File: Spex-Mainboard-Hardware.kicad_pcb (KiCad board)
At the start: 4 copper layers, 94 parts, among them K1 G5LE_1A4_DC3, K2 G5LE_1A4_DC3, P11 SWD Header, P11 USB_OTG, Q11 2N7002K, Q11 BSS215PH6327, Q11 Si5468DC, SW1 SW_PUSH, U1 MKL04Z32VLC4, U11 BME280, U11 LSM9DS1, U11 MCP9808T, U11 MMQA6V2T1G, U11 NUP2201MR6, U111 AT45DB641E, U111 LM4030, U111 MCP2551-I/SN, U111 ST1480ABDR, U13 SCHA4B0419, U3 MK20DX256VLH7, Y11 Crystal

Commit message: Added power board to both sch and pcb. Will route when ready for it
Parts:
- removed C111 (x3), C211: C, Capacitors_SMD:C_0603
- removed C111: .1uF, Capacitors_SMD:C_0603
- removed C111 (x3): 100nF, Capacitors_SMD:C_0603
- removed C111: 10nF, Capacitors_SMD:C_0603
- removed C111: 4.7uF, Capacitors_SMD:C_0603
- removed C111, C211: 10uF, Capacitors_SMD:C_0603
- removed D11 (x4): LED, LEDs:LED_0603
- removed D11 (x2): FM5819-W, Diodes_SMD:SMA_Standard
- removed P11: USB_OTG, Connect:USB_Micro-B
- removed P11: SWD Header, SPEX_Parts:SWD-10
- removed Q11 (x2): 2N7002K, TO_SOT_Packages_SMD:SOT-23
- removed Q11: BSS215PH6327, TO_SOT_Packages_SMD:SOT-23
- removed Q11 (x3): Si5468DC, SPEX_Parts:ChipFet-8
- removed R111 (x2): 1K, Resistors_SMD:R_0603
- removed R111 (x3), R211 (x9): R, Resistors_SMD:R_0603
- removed R111, R211, R311 (x2): 10K, Resistors_SMD:R_0603
- removed R111, R311 (x5): 10k, Resistors_SMD:R_0603
- removed R111 (x3): 12k, Resistors_SMD:R_0603
- removed R311 (x2): 120, Resistors_SMD:R_0603
- removed TH11 (x3): THERMISTOR, Connect:PINHEAD1-2
- removed U111: LM4030, TO_SOT_Packages_SMD:SOT-23-5
- removed U111: MCP2551-I/SN, Power_Integrations:SO-8
- removed U111: ST1480ABDR, Power_Integrations:SO-8
- removed U111: AT45DB641E, SMD_Packages:SOIC-8-N
- removed Y11: Crystal, SPEX_Parts:CX3225GB16000D0HPQCC
- added C1: 1uF, Capacitors_SMD:C_0603, F.Cu at (98.0, -35.6)
- added C10: C, Capacitors_SMD:C_0603, F.Cu at (159.8, -25.8)
- added C105: 47uf, Capacitors_SMD:C_1206, F.Cu at (270.7, -7.50)
- added C109: 100nf, Capacitors_SMD:C_0402, F.Cu at (268.0, 4.40)
- added C114: 22uf, Capacitors_SMD:C_1206, F.Cu at (258.6, -0.90)
- added C118: 22uf, Capacitors_SMD:C_1206, F.Cu at (306.4, -35.0)
- added C119: 1uf 100v, Capacitors_SMD:C_1206, F.Cu at (263.9, -35.0)
- added C12: 10nF, Capacitors_SMD:C_0603, F.Cu at (147.8, -14.1)
- added C120: .1uf 100v, Capacitors_SMD:C_1206, F.Cu at (236.8, -20.9)
- added C121: 100nf, Capacitors_SMD:C_0603, F.Cu at (306.3, -28.7)
- added C122: 47uf, Capacitors_SMD:C_1206, F.Cu at (293.4, -27.1)
- added C123: 1uf 100v, Capacitors_SMD:C_1206, F.Cu at (244.4, -17.4)
- added C13: 100nF, Capacitors_SMD:C_0603, F.Cu at (152.5, -14.1)
- added C14: 4.7uF, Capacitors_SMD:C_0603, F.Cu at (140.4, -10.2)
- added C15: 100nF, Capacitors_SMD:C_0603, F.Cu at (153.1, -20.0)
- added C16: 10uF, Capacitors_SMD:C_0603, F.Cu at (155.9, -25.8)
- added C17: C, Capacitors_SMD:C_0603, F.Cu at (92.4, -13.4)
- added C18: C, Capacitors_SMD:C_0603, F.Cu at (85.9, -6.64)
- added C19: .1uF, Capacitors_SMD:C_0603, F.Cu at (94.8, -19.2)
- added C2: 1uF, Capacitors_SMD:C_0603, F.Cu at (115.0, -56.9)
- added C20: 10uF, Capacitors_SMD:C_0603, F.Cu at (98.7, -19.2)
- added C21: C, Capacitors_SMD:C_0603, F.Cu at (105.9, -46.6)
- added C3: 1uF, Capacitors_SMD:C_0603, F.Cu at (98.0, -41.5)
- added C4: 1uF, Capacitors_SMD:C_0603, F.Cu at (109.3, -51.0)
- added C5: 2.2uF, Capacitors_SMD:C_0603, F.Cu at (119.0, -56.9)
- added C6: .1uF, Capacitors_SMD:C_0603, F.Cu at (108.1, -56.9)
- added C7: C, Capacitors_SMD:C_0603, F.Cu at (94.7, -38.0)
- added C8: C, Capacitors_SMD:C_0603, F.Cu at (111.7, -56.9)
- added C9: C, Capacitors_SMD:C_0603, F.Cu at (152.1, -25.8)
- added D106: ZENER, Diodes_SMD:SOD-123, F.Cu at (253.9, -25.1)
- added D108: ZENER, Diodes_SMD:SOD-123, F.Cu at (262.9, -28.6)
- added D109: D_Schottky_x2_Serial_AKC, Transistors_SMD:sc70, F.Cu at (241.0, -36.3)
- added D110: DIODE, Diodes_SMD:Diode-SMA_Standard, F.Cu at (256.5, -33.5)
- added F101: FUSE, Fuse_Holders_and_Fuses:Fuse_SMD2920, F.Cu at (238.2, -29.6)
- added L102: 2.2uh, SMD_Packages:SMD-2010_Pol, F.Cu at (264.4, -8.88)
- added L103: 3.3uh, NRS8030:NRS8030T3R3MJGJ, F.Cu at (286.1, -25.7)
- added P1: USB_OTG, Connect:USB_Micro-B, F.Cu at (101.4, -55.3)
- added P2: SWD Header, SPEX_Parts:SWD-10, F.Cu at (77.3, -36.9)
- added Q1: 2N7002K, TO_SOT_Packages_SMD:SOT-23, F.Cu at (103.9, -25.5)
- added Q101: MOS_N_numbered, Housings_SOT-23_SOT-143_TSOT-6:SOT-23, F.Cu at (253.9, -7.55)
- added Q104: MOS_N_numbered, Housings_SOT-23_SOT-143_TSOT-6:SOT-23, F.Cu at (288.1, -35.0)
- added Q105: Si3407DV, Power:Si3407DV, F.Cu at (246.3, -23.3)
- added Q106: Q_PNP_BEC, Housings_SOT-23_SOT-143_TSOT-6:SOT-23, F.Cu at (248.1, -31.5)
- added Q2: 2N7002K, TO_SOT_Packages_SMD:SOT-23, F.Cu at (96.6, -25.5)
- added Q3: BSS215PH6327, TO_SOT_Packages_SMD:SOT-23, F.Cu at (77.6, -25.5)
- added Q4: Si5468DC, SPEX_Parts:ChipFet-8, F.Cu at (84.8, -13.5)
- added Q5: Si5468DC, SPEX_Parts:ChipFet-8, F.Cu at (74.9, -9.06)
- added Q6: Si5468DC, SPEX_Parts:ChipFet-8, F.Cu at (87.0, -23.1)
- added R1: R, Resistors_SMD:R_0603, F.Cu at (117.0, -45.2)
- added R10: 1K, Resistors_SMD:R_0603, F.Cu at (104.9, -40.7)
- added R108: 33.2k, Resistors_SMD:R_0603, F.Cu at (275.6, -7.90)
- added R109: 10k, Resistors_SMD:R_0603, F.Cu at (263.3, 1.72)
- added R12: 10K, Resistors_SMD:R_0603, F.Cu at (115.8, -51.0)
- added R126: 10K, Resistors_SMD:R_0603, F.Cu at (267.7, -1.25)
- added R13: 10k, Resistors_SMD:R_0603, F.Cu at (101.4, -41.5)
- added R130: 10K, Resistors_SMD:R_0603, F.Cu at (263.3, -4.13)
- added R14: 12k, Resistors_SMD:R_0603, F.Cu at (134.9, -8.79)
- added R140: 10K, Resistors_SMD:R_0603, F.Cu at (302.8, -22.9)
- added R141: 10K, Resistors_SMD:R_0603, F.Cu at (311.1, -35.4)
- added R145: 10k, Resistors_SMD:R_0603, F.Cu at (298.1, -21.7)
- added R146: 33.2k, Resistors_SMD:R_0603, F.Cu at (254.8, -16.7)
- added R147: 56.2k, Resistors_SMD:R_0603, F.Cu at (298.3, -27.5)
- added R148: 10, Resistors_SMD:R_0603, F.Cu at (267.8, -28.7)
- added R149: 27.4k, Resistors_SMD:R_0603, F.Cu at (274.6, -35.4)
- added R15: 12k, Resistors_SMD:R_0603, F.Cu at (148.8, -20.0)
- added R150: 10, Resistors_SMD:R_0603, F.Cu at (258.7, -22.6)
- added R151: 10.2k, Resistors_SMD:R_0603, F.Cu at (269.9, -35.4)
- added R152: 100k, Resistors_SMD:R_0603, F.Cu at (250.3, -17.8)
- added R16: 12k, Resistors_SMD:R_0603, F.Cu at (131.5, -8.79)
- added R17: R, Resistors_SMD:R_0603, F.Cu at (148.8, -25.8)
- added R18: R, Resistors_SMD:R_0603, F.Cu at (80.1, 8.73)
- added R19: R, Resistors_SMD:R_0603, F.Cu at (83.6, 8.73)
- added R2: 10K, Resistors_SMD:R_0603, F.Cu at (112.3, -39.3)
- added R20: R, Resistors_SMD:R_0603, F.Cu at (87.0, 2.88)
- added R21: R, Resistors_SMD:R_0603, F.Cu at (90.5, 2.88)
- added R22: R, Resistors_SMD:R_0603, F.Cu at (87.0, 8.73)
- added R23: R, Resistors_SMD:R_0603, F.Cu at (73.2, 8.73)
- added R24: R, Resistors_SMD:R_0603, F.Cu at (90.5, 8.73)
- added R25: R, Resistors_SMD:R_0603, F.Cu at (80.1, 2.88)
- added R26: R, Resistors_SMD:R_0603, F.Cu at (76.7, 8.73)
- added R27: R, Resistors_SMD:R_0603, F.Cu at (83.6, 2.88)
- added R28: R, Resistors_SMD:R_0603, F.Cu at (82.5, -6.64)
- added R29: 10K, Resistors_SMD:R_0603, F.Cu at (109.3, -25.8)
- added R3: 33, Resistors_SMD:R_0603, F.Cu at (109.1, -39.3)
- added R30: 10k, Resistors_SMD:R_0603, F.Cu at (89.4, -6.64)
- added R31: 10k, Resistors_SMD:R_0603, F.Cu at (95.8, -13.4)
- added R32: 120, Resistors_SMD:R_0603, F.Cu at (102.6, -19.2)
- added R33: 120, Resistors_SMD:R_0603, F.Cu at (109.3, -20.0)
- added R34: 10K, Resistors_SMD:R_0603, F.Cu at (99.3, -13.4)
- added R35: 10k, Resistors_SMD:R_0603, F.Cu at (92.8, -7.50)
- added R36: 10k, Resistors_SMD:R_0603, F.Cu at (112.8, -25.8)
- added R37: 10k, Resistors_SMD:R_0603, F.Cu at (106.0, -14.1)
- added R38: 10K, Resistors_SMD:R_0603, F.Cu at (112.8, -20.0)
- added R39: R, Resistors_SMD:R_0603, F.Cu at (73.2, 2.88)
- added R4: 33, Resistors_SMD:R_0603, F.Cu at (119.0, -51.0)
- added R40: R, Resistors_SMD:R_0603, F.Cu at (76.7, 2.88)
- added R5: 4.7K, Resistors_SMD:R_0603, F.Cu at (105.6, -34.9)
- added R6: 4.7K, Resistors_SMD:R_0603, F.Cu at (101.7, -34.9)
- added R7: 4.7K, Resistors_SMD:R_0603, F.Cu at (113.5, -45.2)
- added R8: 4.7K, Resistors_SMD:R_0603, F.Cu at (109.6, -45.2)
- added R9: 1K, Resistors_SMD:R_0603, F.Cu at (112.5, -51.0)
- added TH1: THERMISTOR, Connect:PINHEAD1-2, F.Cu at (124.9, -23.8)
- added TH2: THERMISTOR, Connect:PINHEAD1-2, F.Cu at (124.9, -14.0)
- added TH3: THERMISTOR, Connect:PINHEAD1-2, F.Cu at (134.6, -23.8)
- added U10: LM4030, TO_SOT_Packages_SMD:SOT-23-5, F.Cu at (142.6, -16.5)
- added U105: TPS563200, Housings_SOT-23_SOT-143_TSOT-6:SOT-23-6, F.Cu at (251.6, -0.30)
- added U108: TPS563200, Housings_SOT-23_SOT-143_TSOT-6:SOT-23-6, F.Cu at (299.4, -34.4)
- added U12: ST1480ABDR, Power_Integrations:SO-8, F.Cu at (76.5, -18.3)
- added U14: AT45DB641E, SMD_Packages:SOIC-8-N, F.Cu at (88.1, -36.9)
- added U2: NUP2201MR6, SPEX_Parts:TSOP-6, F.Cu at (77.8, -45.5)
- added U4: NUP2201MR6, SPEX_Parts:TSOP-6, F.Cu at (77.8, -55.0)
- added U5: NUP2201MR6, SPEX_Parts:TSOP-6, F.Cu at (90.3, -55.0)
- added U6: MMQA6V2T1G, SPEX_Parts:TSOP-6, F.Cu at (90.1, -45.5)
- added U7: MCP9808T, Housings_SSOP:MSOP-8_3x3mm_Pitch0.65mm, F.Cu at (133.9, -15.3)
- added U8: BME280, SPEX_Parts:LGA-8, F.Cu at (143.2, -24.9)
- added U9: LSM9DS1, SPEX_Parts:LGA-24, F.Cu at (156.2, -19.5)
- added Y1: Crystal, SPEX_Parts:CX3225GB16000D0HPQCC, F.Cu at (100.8, -46.9)
- C11: value 1uF -> 100nF
- R11: value R -> 1K
- U11: value NUP2201MR6 -> MCP2551-I/SN; footprint SPEX_Parts:TSOP-6 -> Power_Integrations:SO-8
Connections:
- K1 pad 3: /Data_Input_Output/Battery_Out -> (no net)
- K2 pad 3: /Data_Input_Output/User_Out -> (no net)
- R11 pad 1: Net-(P1-Pad1) -> LED_Status_2
- R11 pad 2: Net-(D1-Pad2) -> (no net)
- U1 pad 1: Net-(U1-Pad1) -> (no net)
- U1 pad 11: Net-(U1-Pad11) -> (no net)
- U1 pad 12: Net-(U1-Pad12) -> (no net)
- U1 pad 13: Net-(U1-Pad13) -> (no net)
- U1 pad 14: Net-(U1-Pad14) -> (no net)
- U1 pad 19: Net-(U1-Pad19) -> (no net)
- U1 pad 2: Net-(U1-Pad2) -> (no net)
- U1 pad 20: Net-(U1-Pad20) -> (no net)
- U1 pad 21: Net-(U1-Pad21) -> (no net)
- U1 pad 22: Net-(U1-Pad22) -> (no net)
- U1 pad 23: Net-(U1-Pad23) -> (no net)
- U1 pad 24: Net-(U1-Pad24) -> (no net)
- U1 pad 25: /PTB5 -> (no net)
- U1 pad 26: Net-(U1-Pad26) -> (no net)
- U1 pad 27: Net-(U1-Pad27) -> (no net)
- U1 pad 28: Net-(U1-Pad28) -> (no net)
- U1 pad 29: Net-(U1-Pad29) -> (no net)
- U1 pad 30: Net-(U1-Pad30) -> (no net)
- U1 pad 31: Net-(U1-Pad31) -> (no net)
- U1 pad 32: Net-(U1-Pad32) -> (no net)
- U1 pad 7: Net-(U1-Pad7) -> (no net)
- U1 pad 9: Net-(U1-Pad9) -> (no net)
- U11 pad 1: Net-(P1-Pad3) -> CAN0_TX
- U11 pad 3: Net-(U2-Pad3) -> +3V3
- U11 pad 4: Net-(U2-Pad4) -> CAN0_RX
- U11 pad 5: Net-(R2-Pad1) -> (no net)
- U11 pad 6: Net-(P1-Pad2) -> /Data_Input_Output/CANL_out
- U3 pad 12: Net-(U3-Pad12) -> (no net)
- U3 pad 18: Net-(U3-Pad18) -> (no net)
- U3 pad 19: Net-(U3-Pad19) -> (no net)
- U3 pad 20: Net-(U3-Pad20) -> (no net)
- U3 pad 26: Net-(U3-Pad26) -> (no net)
- U3 pad 27: Net-(U3-Pad27) -> (no net)
- U3 pad 42: Net-(U3-Pad42) -> (no net)
- U3 pad 43: Net-(U3-Pad43) -> (no net)
- U3 pad 45: SD_Detect -> (no net)
- U3 pad 49: SPI0_CS0 -> (no net)
- U3 pad 59: UART2_RX -> (no net)
- U3 pad 60: UART2_TX -> (no net)
- U3 pad 61: Net-(U3-Pad61) -> (no net)
- U3 pad 62: Net-(U3-Pad62) -> (no net)
- U3 pad 63: Net-(U3-Pad63) -> (no net)
- U3 pad 64: Net-(U3-Pad64) -> (no net)
- U3 pad 8: Net-(U3-Pad8) -> (no net)

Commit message: working on PCB layout
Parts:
- moved SW1 253.8 mm to (117.5, 101.7), turned to 180 degrees
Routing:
- net /PTB1: track 0.00 -> 13.2 mm, vias 0 -> 2
- net /PTA4: track 0.00 -> 12.8 mm
- net /PTA6: track 0.00 -> 9.59 mm, vias 0 -> 2
- net /PTB2: track 0.00 -> 8.17 mm
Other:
- net class Default: clearance 0.2 -> 0.15; via_dia 0.6 -> 0.508; via_drill 0.4 -> 0.381
- net class Power added: clearance 0.2, trace_width 0.25, via_dia 0.5, via_drill 0.4
- rule trace_clearance: 0.2 -> 0.15

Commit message: board now 80% laid out
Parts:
- removed the C11 at (-68.1, 53.1)
- removed the C11 at (-84.7, 69.4)
- removed the C11 at (-72.6, 47.2)
- removed the C11 at (-88.1, 66.2)
- removed the C11 at (-82.8, 63.5)
- removed the C11 at (-75.1, 58.3)
- removed the C11 at (-71.5, 53.1)
- removed the C11 at (-88.1, 72.1)
- removed the C11 at (-26.6, 17.6)
- removed C7, C8: C, Capacitors_SMD:C_0603
- removed the R11 at (-78.7, 63.5)
- removed the R11 at (-75.3, 64.2)
- removed the R11 at (-64.6, 53.1)
- removed the R11 at (-81.2, 69.4)
- removed the R11 at (-71.3, 59.0)
- removed the R11 at (-84.4, 75.3)
- removed the R11 at (-68.9, 47.2)
- removed the R11 at (-69.7, 70.8)
- removed the R11 at (-73.4, 70.8)
- removed the U11 at (-99.9, 101.2)
- removed the U11 at (-112.5, 101.2)
- removed the U11 at (-100.1, 110.7)
- removed the U11 at (160.8, 95.5)
- removed the U7 at (133.9, -15.3)
- removed the U8 at (143.2, -24.9)
- added C11: 100nF, Capacitors_SMD:C_0603, F.Cu at (127.9, 78.6)
- added C22: C, Capacitors_SMD:C_0603, F.Cu at (137.5, 71.1)
- added D1: LED, LEDs:LED_0603, F.Cu at (86.8, 67.2)
- added D2: LED, LEDs:LED_0603, F.Cu at (104.4, 54.0)
- added D3: LED, LEDs:LED_0603, F.Cu at (106.7, 54.1)
- added D4: LED, LEDs:LED_0603, F.Cu at (109.0, 54.1)
- added D5: FM5819-W, Diodes_SMD:SMA_Standard, F.Cu at (89.8, 110.5)
- added D6: FM5819-W, Diodes_SMD:SMA_Standard, F.Cu at (120.1, 110.6)
- added R11: 1K, Resistors_SMD:R_0603, F.Cu at (109.0, 56.9)
- R1: value R -> 1K
- moved U11 286.7 mm to (170.6, 64.9)
- moved R18 197.0 mm to (267.6, 69.4)
- moved R19 197.0 mm to (271.0, 69.4)
- moved R20 197.0 mm to (274.5, 63.5)
- moved R21 197.0 mm to (277.9, 63.5)
- moved R22 197.0 mm to (274.5, 69.4)
- moved R23 197.0 mm to (260.7, 69.4)
- moved R24 197.0 mm to (277.9, 69.4)
- moved R25 197.0 mm to (267.6, 63.5)
- moved R26 197.0 mm to (264.1, 69.4)
- moved R27 197.0 mm to (271.0, 63.5)
- moved R39 197.0 mm to (260.7, 63.5)
- moved R40 197.0 mm to (264.1, 63.5)
- moved Q6 155.0 mm to (170.0, 107.8)
- moved Q5 146.6 mm to (169.8, 102.6)
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- renumbered U11 to U7, U11 to U8
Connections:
- net /Power Distribution/3v3 renamed /Power Distribution/12Vto3v3.sch/Vout
- net /Power Distribution/5v renamed /Power Distribution/12Vto5V.sch/Vout
- C114 pad 2: /Power Distribution/VBUS -> /Power Distribution/VBus
- C118 pad 2: /Power Distribution/VBUS -> /Power Distribution/VBus
- C120 pad 1: /Power Distribution/VBUS -> /Power Distribution/VBus
- C9 pad 1: Net-(C9-Pad1) -> +3V3
- K1 pad 3: (no net) -> /Data_Input_Output/Battery_Out
- K2 pad 3: (no net) -> /Data_Input_Output/User_Out
- P2 pad 10: (no net) -> /RESET_b
- P2 pad 6: (no net) -> Net-(P2-Pad6)
- P2 pad 7: (no net) -> Net-(P2-Pad7)
- P2 pad 8: (no net) -> Net-(P2-Pad8)
- P2 pad 9: (no net) -> Net-(P2-Pad9)
- Q101 pad 1: /Power Distribution/VBUS -> /Power Distribution/VBus
- Q104 pad 1: /Power Distribution/VBUS -> /Power Distribution/VBus
- Q105 pad 1: /Power Distribution/VBUS -> /Power Distribution/VBus
- Q105 pad 2: /Power Distribution/VBUS -> /Power Distribution/VBus
- Q105 pad 5: /Power Distribution/VBUS -> /Power Distribution/VBus
- Q105 pad 6: /Power Distribution/VBUS -> /Power Distribution/VBus
- Q3 pad 3: (no net) -> Net-(Q3-Pad3)
- R1 pad 2: (no net) -> Net-(D1-Pad2)
- R10 pad 2: (no net) -> Net-(D3-Pad2)
- R126 pad 2: /Power Distribution/VBUS -> /Power Distribution/VBus
- R130 pad 1: /Power Distribution/VBUS -> /Power Distribution/VBus
- R140 pad 2: /Power Distribution/VBUS -> /Power Distribution/VBus
- R141 pad 1: /Power Distribution/VBUS -> /Power Distribution/VBus
- R18 pad 1: /Power Distribution/VBUS -> /Power Distribution/VBus
- R18 pad 2: (no net) -> /Power Distribution/VBus
- R19 pad 2: (no net) -> VBatt
- R20 pad 1: (no net) -> Net-(R20-Pad1)
- R20 pad 2: (no net) -> /Power Distribution/Bat1-2
- R21 pad 1: (no net) -> Net-(R21-Pad1)
- R21 pad 2: (no net) -> /Power Distribution/Bat2-3
- R23 pad 1: (no net) -> Net-(R23-Pad1)
- R24 pad 1: (no net) -> Net-(R24-Pad1)
- R25 pad 1: (no net) -> Net-(R25-Pad1)
- R25 pad 2: (no net) -> /Power Distribution/PowIRQ
- R39 pad 2: (no net) -> +5V
- U1 pad 1: (no net) -> Net-(U1-Pad1)
- U1 pad 11: (no net) -> Net-(U1-Pad11)
- U1 pad 12: (no net) -> Net-(U1-Pad12)
- U1 pad 13: (no net) -> Net-(U1-Pad13)
- U1 pad 14: (no net) -> Net-(U1-Pad14)
- U1 pad 19: (no net) -> Net-(U1-Pad19)
- U1 pad 2: (no net) -> Net-(U1-Pad2)
- U1 pad 20: (no net) -> Net-(U1-Pad20)
- U1 pad 21: (no net) -> Net-(U1-Pad21)
- U1 pad 22: (no net) -> Net-(U1-Pad22)
- U1 pad 23: (no net) -> Net-(U1-Pad23)
- U1 pad 24: (no net) -> Net-(U1-Pad24)
- U1 pad 25: (no net) -> /PTB5
- U1 pad 26: (no net) -> Net-(U1-Pad26)
- U1 pad 27: (no net) -> Net-(U1-Pad27)
- U1 pad 28: (no net) -> Net-(U1-Pad28)
- U1 pad 29: (no net) -> Net-(U1-Pad29)
- U1 pad 30: (no net) -> Net-(U1-Pad30)
- U1 pad 31: (no net) -> Net-(U1-Pad31)
- U1 pad 32: (no net) -> Net-(U1-Pad32)
- U1 pad 7: (no net) -> Net-(U1-Pad7)
- U1 pad 9: (no net) -> Net-(U1-Pad9)
- U10 pad 1: (no net) -> Net-(U10-Pad1)
- U10 pad 3: (no net) -> Net-(U10-Pad3)
- U105 pad 3: /Power Distribution/VBUS -> /Power Distribution/VBus
- U108 pad 3: /Power Distribution/VBUS -> /Power Distribution/VBus
- U11 pad 5: (no net) -> Net-(U11-Pad5)
- U14 pad 3: (no net) -> Net-(U14-Pad3)
- U14 pad 5: (no net) -> Net-(U14-Pad5)
- U2 pad 3: (no net) -> Net-(U2-Pad3)
- U2 pad 4: (no net) -> Net-(U2-Pad4)
- U3 pad 12: (no net) -> Net-(U3-Pad12)
- U3 pad 18: (no net) -> Net-(U3-Pad18)
- U3 pad 19: (no net) -> Net-(U3-Pad19)
- U3 pad 20: (no net) -> Net-(U3-Pad20)
- U3 pad 26: (no net) -> Net-(U3-Pad26)
- U3 pad 27: (no net) -> Net-(U3-Pad27)
- U3 pad 42: (no net) -> Net-(U3-Pad42)
- U3 pad 43: (no net) -> Net-(U3-Pad43)
- U3 pad 45: (no net) -> SD_Detect
- U3 pad 49: (no net) -> SPI0_CS0
- U3 pad 59: (no net) -> UART2_RX
- U3 pad 60: (no net) -> UART2_TX
- U3 pad 61: (no net) -> Net-(U3-Pad61)
- U3 pad 62: (no net) -> Net-(U3-Pad62)
- U3 pad 63: (no net) -> Net-(U3-Pad63)
- U3 pad 64: (no net) -> Net-(U3-Pad64)
- U3 pad 8: (no net) -> Net-(U3-Pad8)
- U6 pad 1: SPI0_CS -> SPI0_CS0
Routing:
- net GND: track 0.00 -> 147.3 mm, vias 0 -> 27
- net +3V3: track 0.00 -> 111.8 mm, vias 0 -> 18
- net Temp3: track 0.00 -> 46.8 mm, vias 0 -> 1
- net Temp2: track 0.00 -> 40.6 mm, vias 0 -> 1
- net Temp1: track 0.00 -> 33.9 mm, vias 0 -> 1
- net I2C0_SCL: track 0.00 -> 28.0 mm, vias 0 -> 4
- net I2C0_SDA: track 0.00 -> 26.7 mm
- net /PTA6: track 9.59 -> 32.9 mm, vias 2 -> 4
- net /HAB Sensors/2.5VRefVoltage: track 0.00 -> 23.0 mm
- net SPI0_MISO: track 0.00 -> 21.5 mm
- net SD_CTRL: track 0.00 -> 18.0 mm
- net Net-(D5-Pad2): track 0.00 -> 16.7 mm
- net Net-(D6-Pad2): track 0.00 -> 16.4 mm
- net SPI0_MOSI: track 0.00 -> 15.3 mm, vias 0 -> 2
- net (no net): track 0.00 -> 14.1 mm
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- added copper zone on In2.Cu, net +3V3
- added copper zone on B.Cu, net GND
- added copper zone on In1.Cu, net GND
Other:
- board outline added: 100 x 80 mm

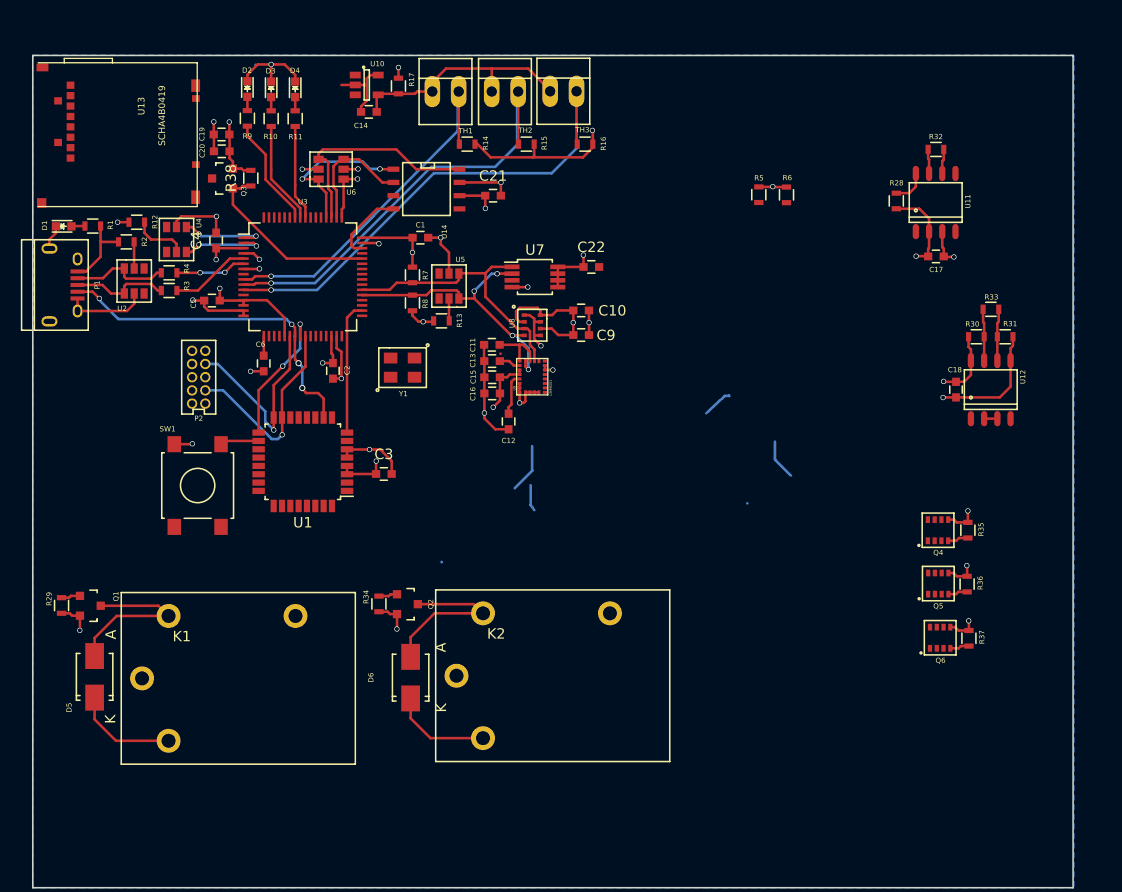
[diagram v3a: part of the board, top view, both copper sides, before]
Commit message: continued PCB layout, small schematic changes
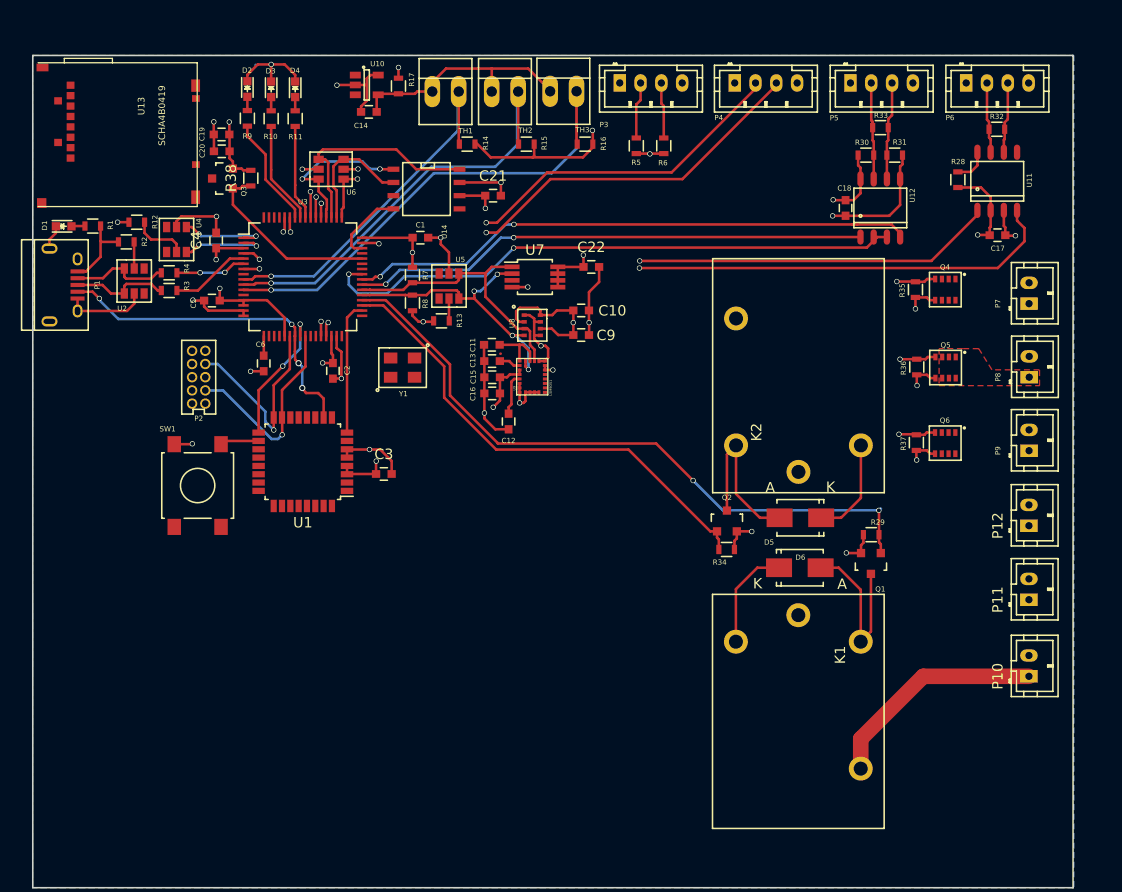
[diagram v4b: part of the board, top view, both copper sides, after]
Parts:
- added P10: CONN_01X02, Connectors_JST:JST_PH_B2B-PH-K_02x2.00mm_Straight, F.Cu at (179.6, 110.5)
- added P11: CONN_01X02, Connectors_JST:JST_PH_B2B-PH-K_02x2.00mm_Straight, F.Cu at (179.6, 103.1)
- added P12: CONN_01X02, Connectors_JST:JST_PH_B2B-PH-K_02x2.00mm_Straight, F.Cu at (179.6, 96.0)
- added P3: CONN_01X04, Connectors_JST:JST_PH_B4B-PH-K_04x2.00mm_Straight, F.Cu at (140.2, 53.5)
- added P4: CONN_01X04, Connectors_JST:JST_PH_B4B-PH-K_04x2.00mm_Straight, F.Cu at (151.3, 53.5)
- added P5: CONN_01X04, Connectors_JST:JST_PH_B4B-PH-K_04x2.00mm_Straight, F.Cu at (162.4, 53.5)
- added P6: CONN_01X04, Connectors_JST:JST_PH_B4B-PH-K_04x2.00mm_Straight, F.Cu at (173.5, 53.5)
- added P7: CONN_01X02, Connectors_JST:JST_PH_B2B-PH-K_02x2.00mm_Straight, F.Cu at (179.6, 74.7)
- added P8: CONN_01X02, Connectors_JST:JST_PH_B2B-PH-K_02x2.00mm_Straight, F.Cu at (179.6, 81.7)
- added P9: CONN_01X02, Connectors_JST:JST_PH_B2B-PH-K_02x2.00mm_Straight, F.Cu at (179.6, 88.8)
- moved R29 78.1 mm to (164.4, 96.9), turned to 180 degrees
- moved Q1 75.1 mm to (164.4, 99.6), turned to 180 degrees
- moved D5 68.6 mm to (157.6, 100.1), turned to 0 degrees
- moved K1 55.4 mm to (151.4, 107.2), turned to 270 degrees
- moved K2 45.9 mm to (163.4, 88.3), turned to 90 degrees
- moved D6 40.5 mm to (157.6, 95.2), turned to 180 degrees
- moved R34 33.8 mm to (150.5, 98.3), turned to 0 degrees
- moved Q2 31.7 mm to (150.5, 95.6), turned to 0 degrees
- moved Q4 25.3 mm to (172.6, 72.3), turned to 180 degrees
- moved R35 23.7 mm to (168.7, 73.3), turned to 90 degrees
- moved Q5 23.0 mm to (172.6, 79.8), turned to 180 degrees
- moved R36 21.4 mm to (168.8, 80.8), turned to 90 degrees
- moved Q6 20.9 mm to (172.5, 87.1), turned to 180 degrees
- moved R30 20.4 mm to (163.9, 60.4)
- moved R31 20.4 mm to (166.7, 60.4)
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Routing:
- net CAN0_RX: track 0.00 -> 75.1 mm, vias 0 -> 2
- net CAN0_TX: track 0.00 -> 69.4 mm, vias 0 -> 2
- net Vbus_MOS_CTRL: track 1.88 -> 69.8 mm, vias 0 -> 2
- net 5V_MOS_CTRL: track 1.88 -> 68.2 mm, vias 0 -> 2
- net 3.3V_MOS_CTRL: track 2.01 -> 66.3 mm, vias 0 -> 2
- net Relay1_ctrl: track 1.84 -> 64.3 mm, vias 0 -> 2
- net RX/TX_CTRL: track 1.27 -> 57.0 mm, vias 0 -> 2
- net I2C1_SCL: track 8.45 -> 63.8 mm
- net UART0_TX: track 0.00 -> 54.6 mm, vias 0 -> 2
- net UART2_RX: track 0.00 -> 54.3 mm, vias 0 -> 2
- net UART2_TX: track 0.00 -> 53.3 mm, vias 0 -> 2
- net I2C1_SDA: track 8.36 -> 60.5 mm
- net UART0_RX: track 0.00 -> 50.0 mm, vias 0 -> 2
- net Relay2_ctrl: track 1.81 -> 46.7 mm
- net /Data_Input_Output/User_Out: track 0.00 -> 36.4 mm
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- added copper zone on F.Cu, net /Data_Input_Output/5V_MOS_OUT
